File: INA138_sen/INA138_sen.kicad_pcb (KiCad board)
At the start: 2 copper layers, 18 parts, among them J1 Screw_Terminal_01x02, J2 Screw_Terminal_01x02, J3 Screw_Terminal_01x02, U1 INA138

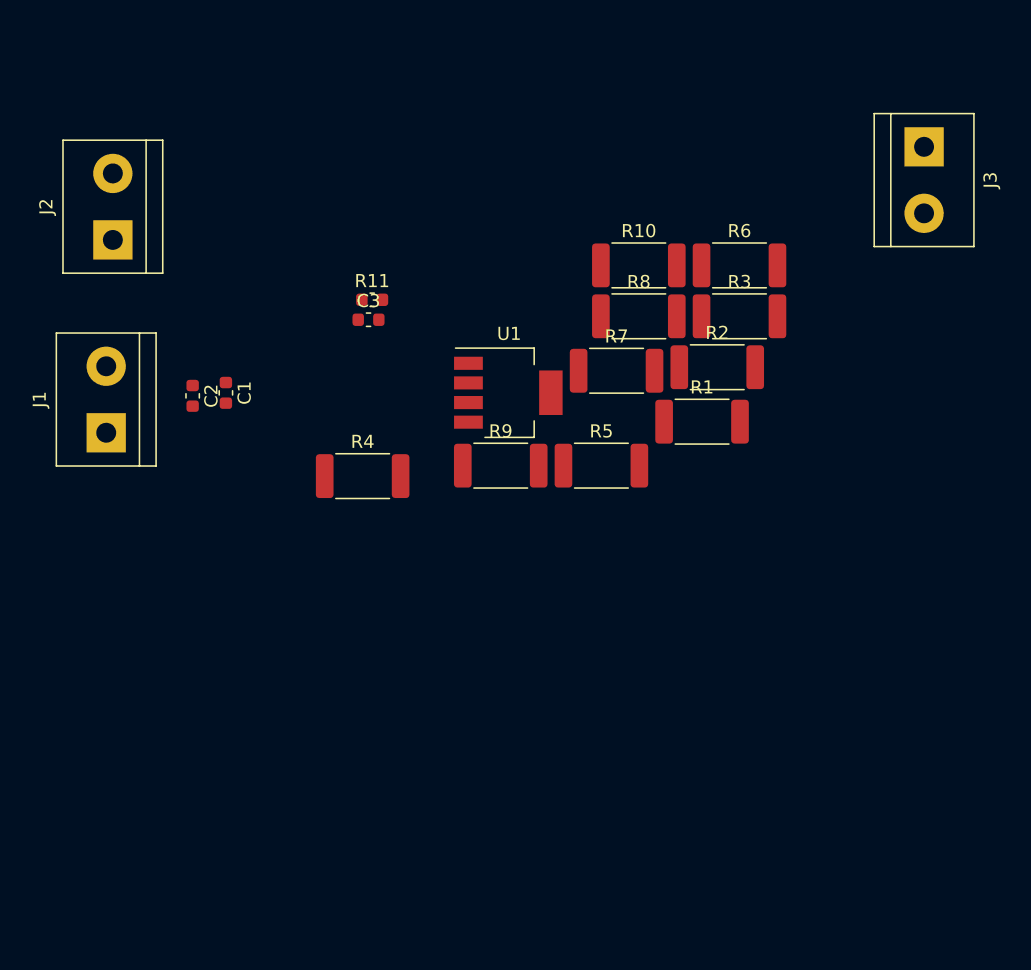
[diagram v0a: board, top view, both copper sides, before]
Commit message: changed footprint of INA138
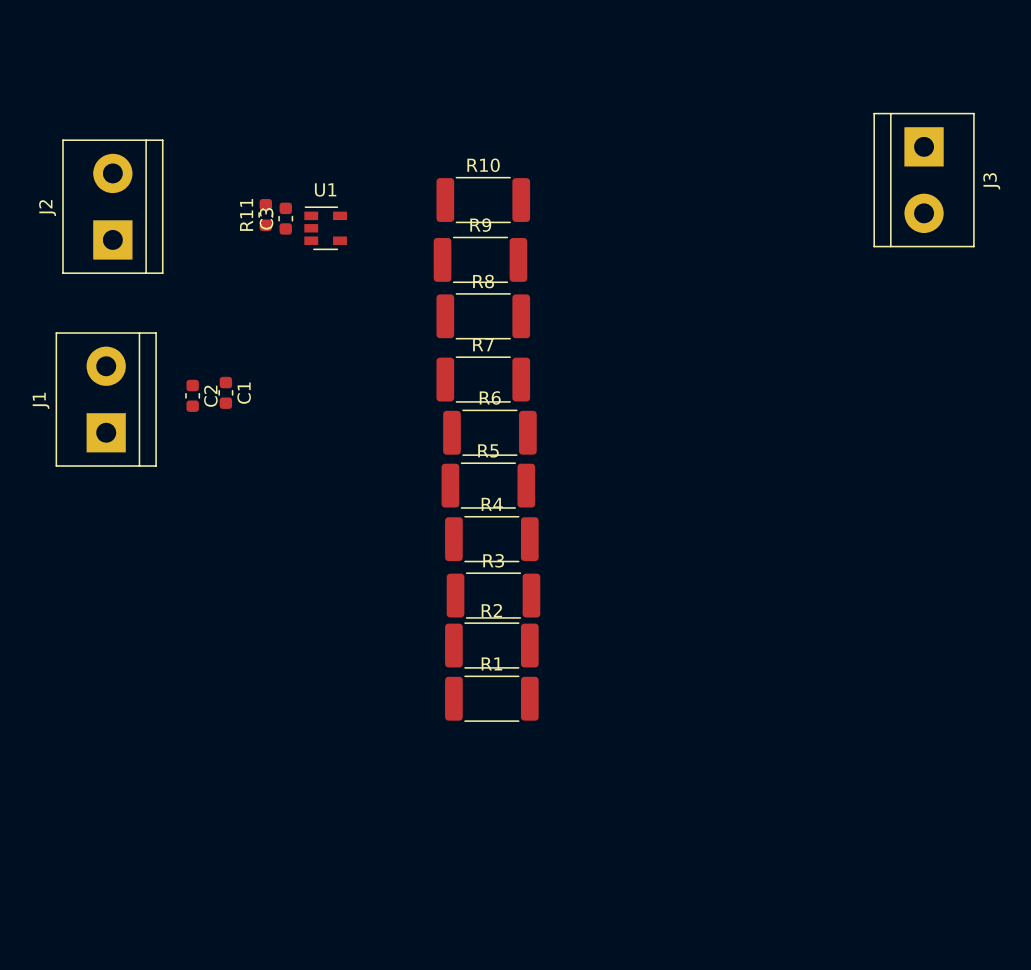
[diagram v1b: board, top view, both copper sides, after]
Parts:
- U1: footprint Package_TO_SOT_SMD:SOT-223-5 -> Package_TO_SOT_SMD:SOT-23-5
- moved R3 28.4 mm to (137.8, 128.8)
- moved R2 27.4 mm to (137.7, 132.6)
- moved R1 26.6 mm to (137.7, 136.7)
- moved R6 23.0 mm to (137.5, 116.3)
- moved U1 18.8 mm to (125.0, 100.7)
- moved R9 15.8 mm to (136.8, 103.1)
- moved R10 12.9 mm to (137.0, 98.6)
- moved R8 11.9 mm to (137.0, 107.4)
- moved R4 11.0 mm to (137.7, 124.5)
- moved R11 10.4 mm to (120.4, 99.7), turned to 90 degrees
- moved R7 10.2 mm to (137.0, 112.3)
- moved C3 9.98 mm to (121.9, 100.0), turned to 90 degrees
- moved R5 8.77 mm to (137.4, 120.4)
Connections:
- C3 pad 1: Net-(C3-Pad1) -> GND
- R11 pad 1: Net-(C3-Pad1) -> GND
- U1 pad 2: Net-(C3-Pad1) -> GND

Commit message: Completed PCB layout
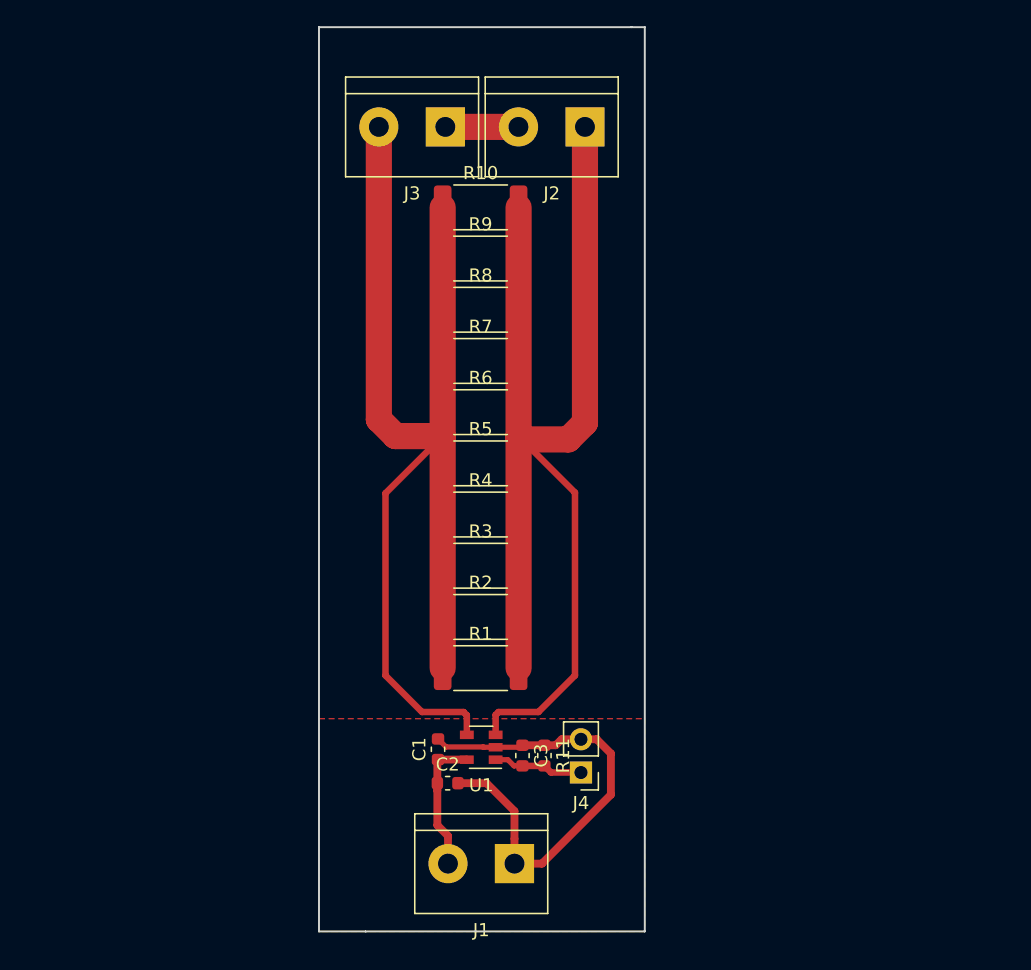
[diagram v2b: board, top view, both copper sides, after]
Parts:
- added J4: Conn_01x02_Female, Connector_PinHeader_2.54mm:PinHeader_1x02_P2.54mm_Vertical, F.Cu at (144.5, 142.3)
- moved R11 46.5 mm to (141.7, 141.0), turned to 270 degrees
- moved J1 45.3 mm to (139.4, 149.3), turned to 180 degrees
- moved C3 44.8 mm to (140.0, 141.0), turned to 270 degrees
- moved U1 41.4 mm to (136.9, 140.4), turned to 180 degrees
- moved J2 37.1 mm to (144.8, 93.0), turned to 180 degrees
- moved J3 36.6 mm to (134.1, 93.0), turned to 180 degrees
- moved C2 35.4 mm to (134.3, 143.1), turned to 0 degrees
- moved C1 31.7 mm to (133.6, 140.5), turned to 90 degrees
- moved R1 2.49 mm to (136.8, 134.3)
- moved R3 2.48 mm to (136.8, 126.5)
- moved R2 2.35 mm to (136.8, 130.4)
- moved R4 2.07 mm to (136.8, 122.6)
- moved R5 1.80 mm to (136.8, 118.7)
- moved R6 1.73 mm to (136.8, 114.8)
- moved R7 1.44 mm to (136.8, 110.8)
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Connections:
- net Net-(C3-Pad2) renamed /VOUT
- net Net-(J2-Pad1) renamed /I+
- net Net-(J3-Pad2) renamed /I-
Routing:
- net /I+: track 0.00 -> 127.5 mm
- net /I-: track 0.00 -> 127.2 mm
- net GND: track 0.00 -> 36.1 mm
- net VCC: track 0.00 -> 10.5 mm
- net /VOUT: track 0.00 -> 6.93 mm
- net Net-(J2-Pad2): track 0.00 -> 5.59 mm
- added copper zone on F.Cu, net GND
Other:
- board outline added: 24.9 x 69.1 mm
- net class Default: clearance 0.2 -> 0.4; trace_width 0.25 -> 0.4
- rule trace_clearance: 0.2 -> 0.4
- rule trace_min: 0.2 -> 0.4
